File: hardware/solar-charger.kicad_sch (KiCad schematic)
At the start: 24 parts, among them J1 Conn_01x02_Male, J2 ISENSE_SOLAR, J3 ISENSE_SOLAR, J4 ISENSE_SOLAR, J5 ISENSE_DISCHARGE, J6 Conn_01x02_Male, Q1 AOI21357, Q2 AOI21357, Q3 AOI21357, Q4 AOI21357, U1 MCP6002-xP, U2 DS3231M

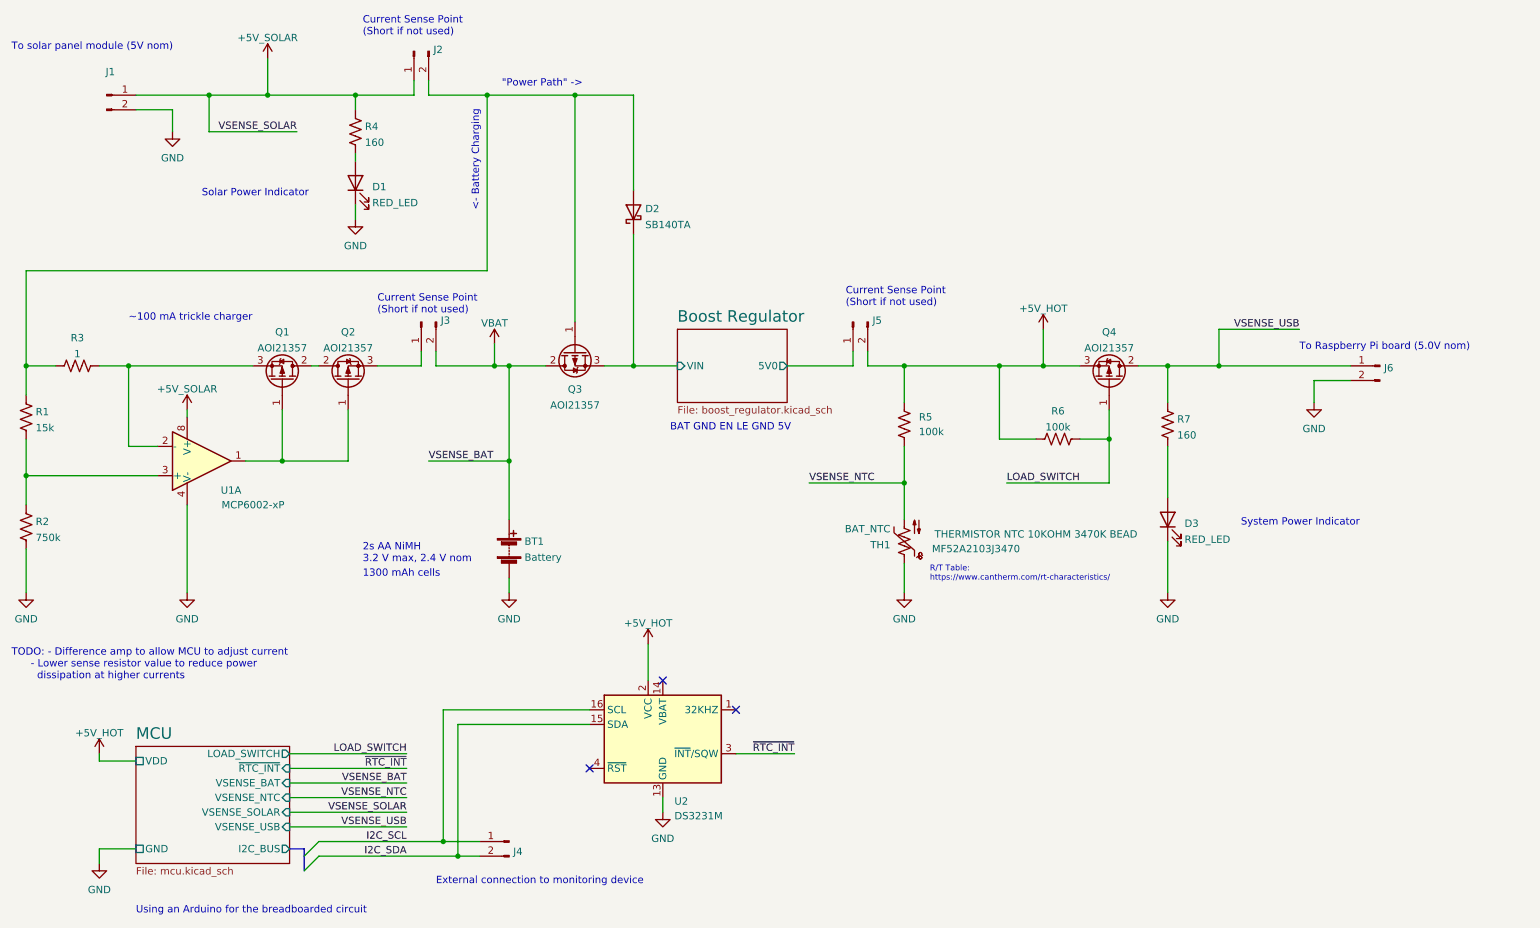
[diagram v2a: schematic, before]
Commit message: hardware: Replace current sense with a schottky, scrap blocking FET Q2
We discovered that we require a diode anyways, so to be a bit more
efficient, replace the fairly large current sense resistor with a
schottky. This required that we updated the voltage divider values to
reflect the new required voltage drop.

Future work here is to consider the worst case highest temperature we
want to support, and then add in a digipot to allow the micro to adjust
the voltage (and therefore the current) up from that point.
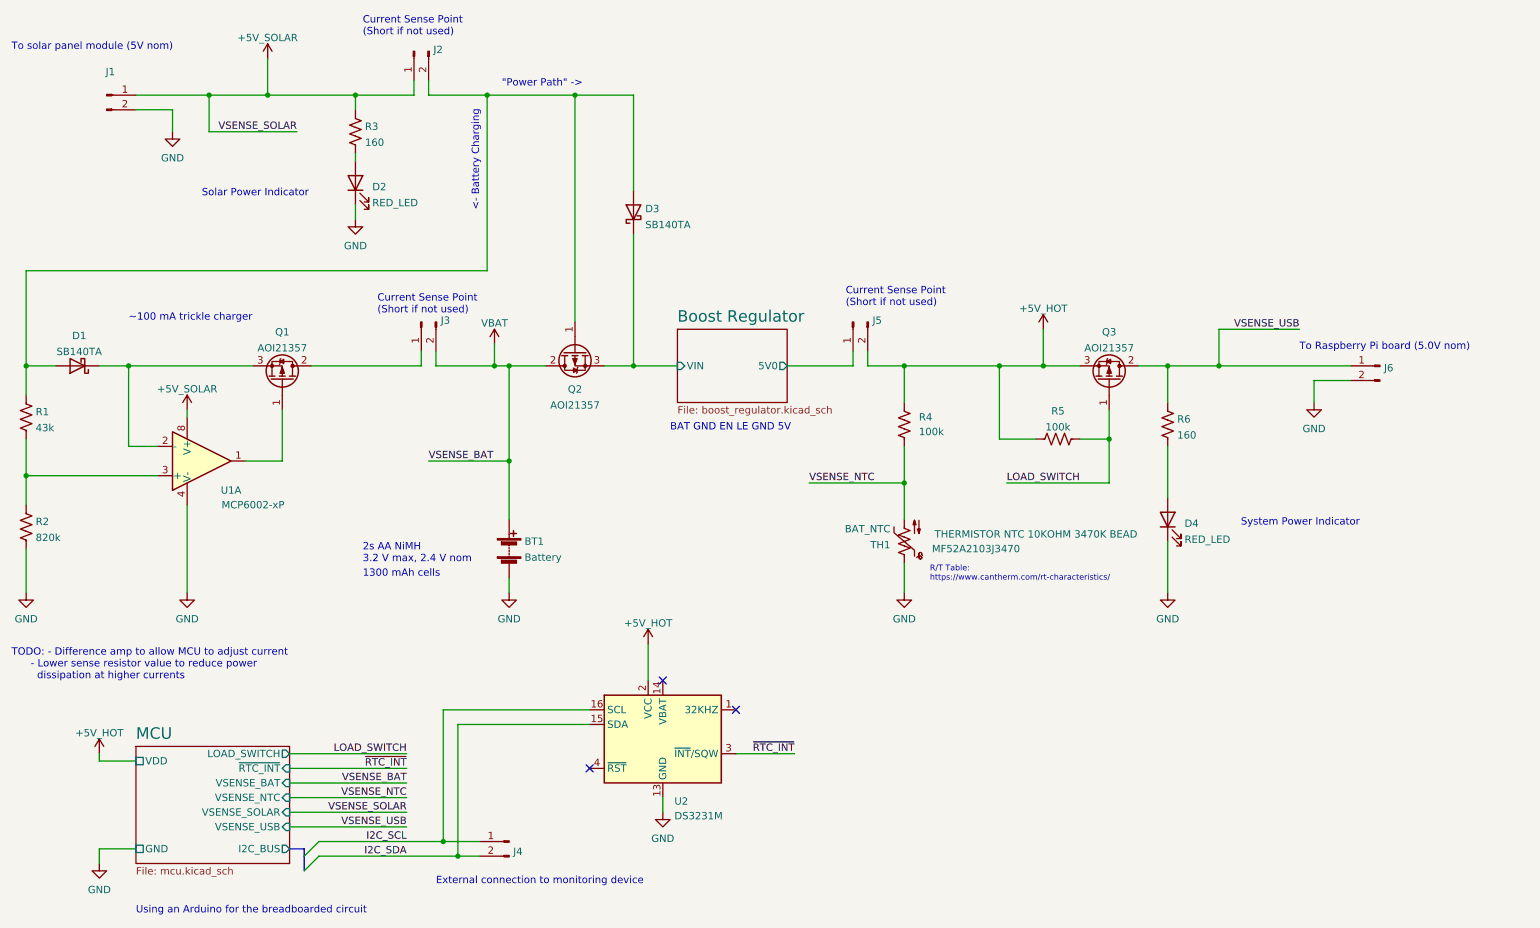
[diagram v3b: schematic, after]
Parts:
- removed Q2: AOI21357, symbol Device:Q_PMOS_GDS
- removed R3: 1, symbol Device:R_US
- added D1: SB140TA, symbol Device:D_Schottky
- R1: value 15k -> 43k
- R2: value 750k -> 820k
- renumbered D1 to D2, D2 to D3, D3 to D4, Q3 to Q2, Q4 to Q3, R4 to R3, R5 to R4, R6 to R5, R7 to R6
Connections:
- net at D3.2 (A), J2.2 (Pin_2), Q2.1 (G)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: now also D1.2 (A)
- net at Q1.3 (S), U1.2 (-): now also D1.1 (K)
- net at Q1.2 (D): now also J3.1 (Pin_1)
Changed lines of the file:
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@@
   (junction (at 232.41 92.71) (diameter 0) (color 0 0 0 0)
-  )
-  (junction (at 69.85 109.22) (diameter 0) (color 0 0 0 0)
   )
   (junction (at 177.8 113.03) (diameter 0) (color 0 0 0 0)
@@
     (stroke (width 0) (type default) (color 0 0 0 0))
   )
-  (wire (pts (xy 81.28 109.22) (xy 81.28 100.33))
-    (stroke (width 0) (type default) (color 0 0 0 0))
-  )
   (wire (pts (xy 125.73 92.71) (xy 130.81 92.71))
     (stroke (width 0) (type default) (color 0 0 0 0))
@@
     (stroke (width 0) (type default) (color 0 0 0 0))
   )
-  (wire (pts (xy 53.34 101.6) (xy 53.34 100.33))
-    (stroke (width 0) (type default) (color 0 0 0 0))
-  )
   (wire (pts (xy 97.79 175.26) (xy 104.14 175.26))
     (stroke (width 0) (type default) (color 0 0 0 0))
@@
     (stroke (width 0) (type default) (color 0 0 0 0))
   )
-  (wire (pts (xy 86.36 92.71) (xy 93.98 92.71))
-    (stroke (width 0) (type default) (color 0 0 0 0))
-  )
   (wire (pts (xy 106.68 92.71) (xy 109.22 92.71))
     (stroke (width 0) (type default) (color 0 0 0 0))
@@
     (stroke (width 0) (type default) (color 0 0 0 0))
   )
+  (wire (pts (xy 53.34 100.33) (xy 53.34 101.6))
+    (stroke (width 0) (type default) (color 0 0 0 0))
+  )
   (wire (pts (xy 57.15 45.72) (xy 57.15 52.07))
     (stroke (width 0) (type default) (color 0 0 0 0))
@@
     (stroke (width 0) (type default) (color 0 0 0 0))
   )
-  (wire (pts (xy 74.93 92.71) (xy 76.2 92.71))
+  (wire (pts (xy 74.93 92.71) (xy 93.98 92.71))
     (stroke (width 0) (type default) (color 0 0 0 0))
   )
@@
   )
   (wire (pts (xy 95.25 43.18) (xy 95.25 45.72))
-    (stroke (width 0) (type default) (color 0 0 0 0))
-  )
-  (wire (pts (xy 69.85 109.22) (xy 81.28 109.22))
     (stroke (width 0) (type default) (color 0 0 0 0))
   )
@@
   )
   (symbol (lib_id "power:+5V_SOLAR") (at 53.34 100.33 0) (unit 1)
-    (in_bom yes) (on_board yes) (fields_autoplaced)
+    (in_bom yes) (on_board yes)
     (property "Reference" "#PWR05" (id 0) (at 53.34 104.14 0)
       (effects (font (size 1.27 1.27)) hide)
@@
   (symbol (lib_id "Device:D_Schottky") (at 130.81 66.04 90) (unit 1)
     (in_bom yes) (on_board yes) (fields_autoplaced)
-    (property "Reference" "D2" (id 0) (at 132.842 65.449 90)
+    (property "Reference" "D3" (id 0) (at 132.842 65.449 90)
       (effects (font (size 1.27 1.27)) (justify right))
     )
@@
       (effects (font (size 1.27 1.27)) (justify left))
     )
-    (property "Value" "15k" (id 1) (at 27.051 103.4666 0)
+    (property "Value" "43k" (id 1) (at 27.051 103.4666 0)
       (effects (font (size 1.27 1.27)) (justify left))
     )
@@
   (symbol (lib_id "Device:R_US") (at 82.55 52.07 0) (unit 1)
     (in_bom yes) (on_board yes) (fields_autoplaced)
-    (property "Reference" "R4" (id 0) (at 84.201 51.1615 0)
+    (property "Reference" "R3" (id 0) (at 84.201 51.1615 0)
       (effects (font (size 1.27 1.27)) (justify left))
     )
@@
   (symbol (lib_id "Device:R_US") (at 177.8 102.87 0) (unit 1)
     (in_bom yes) (on_board yes) (fields_autoplaced)
-    (property "Reference" "R5" (id 0) (at 180.34 101.5999 0)
+    (property "Reference" "R4" (id 0) (at 180.34 101.5999 0)
       (effects (font (size 1.27 1.27)) (justify left))
     )
@@
     (pin "2")
   )
+  (symbol (lib_id "Device:D_Schottky") (at 34.29 92.71 180) (unit 1)
+    (in_bom yes) (on_board yes) (fields_autoplaced)
+    (property "Reference" "D1" (id 0) (at 34.6075 87.4735 0))
+    (property "Value" "SB140TA" (id 1) (at 34.6075 90.2486 0))
+    (property "Footprint" "" (id 2) (at 34.29 92.71 0)
+      (effects (font (size 1.27 1.27)) hide)
+    )
+    (property "Datasheet" "http://www.smc-diodes.com/propdf/SB120%20THRU%20SB160%20N0869%20REV.C.pdf" (id 3) (at 34.29 92.71 0)
+      (effects (font (size 1.27 1.27)) hide)
+    )
+    (pin "1")
+    (pin "2")
+  )
   (symbol (lib_id "Device:Q_PMOS_GDS") (at 213.36 95.25 270) (mirror x) (unit 1)
     (in_bom yes) (on_board yes) (fields_autoplaced)
-    (property "Reference" "Q4" (id 0) (at 213.36 86.8385 90))
+    (property "Reference" "Q3" (id 0) (at 213.36 86.8385 90))
     (property "Value" "AOI21357" (id 1) (at 213.36 89.6136 90))
     (property "Footprint" "" (id 2) (at 215.9 90.17 0)
@@
   (symbol (lib_id "Device:LED") (at 223.52 119.38 90) (unit 1)
     (in_bom yes) (on_board yes) (fields_autoplaced)
-    (property "Reference" "D3" (id 0) (at 226.441 120.059 90)
+    (property "Reference" "D4" (id 0) (at 226.441 120.059 90)
       (effects (font (size 1.27 1.27)) (justify right))
     )
@@
     )
     (property "Datasheet" "~" (id 3) (at 223.52 119.38 0)
-      (effects (font (size 1.27 1.27)) hide)
-    )
-    (pin "1")
-    (pin "2")
-  )
-  (symbol (lib_id "Device:R_US") (at 34.29 92.71 90) (unit 1)
-    (in_bom yes) (on_board yes) (fields_autoplaced)
-    (property "Reference" "R3" (id 0) (at 34.29 87.8545 90))
-    (property "Value" "1" (id 1) (at 34.29 90.6296 90))
-    (property "Footprint" "" (id 2) (at 34.544 91.694 90)
-      (effects (font (size 1.27 1.27)) hide)
-    )
-    (property "Datasheet" "~" (id 3) (at 34.29 92.71 0)
       (effects (font (size 1.27 1.27)) hide)
     )
@@
   (symbol (lib_id "Device:R_US") (at 204.47 105.41 90) (unit 1)
     (in_bom yes) (on_board yes) (fields_autoplaced)
-    (property "Reference" "R6" (id 0) (at 204.47 100.5545 90))
+    (property "Reference" "R5" (id 0) (at 204.47 100.5545 90))
     (property "Value" "100k" (id 1) (at 204.47 103.3296 90))
     (property "Footprint" "" (id 2) (at 204.724 104.394 90)
@@
     )
     (pin "1")
-  )
-  (symbol (lib_id "Device:Q_PMOS_GDS") (at 81.28 95.25 90) (unit 1)
-    (in_bom yes) (on_board yes) (fields_autoplaced)
-    (property "Reference" "Q2" (id 0) (at 81.28 86.8385 90))
-    (property "Value" "AOI21357" (id 1) (at 81.28 89.6136 90))
-    (property "Footprint" "" (id 2) (at 78.74 90.17 0)
-      (effects (font (size 1.27 1.27)) hide)
-    )
-    (property "Datasheet" "~" (id 3) (at 81.28 95.25 0)
-      (effects (font (size 1.27 1.27)) hide)
-    )
-    (pin "1")
-    (pin "2")
-    (pin "3")
   )
   (symbol (lib_id "power:GND") (at 109.22 132.08 0) (unit 1)
@@
   (symbol (lib_id "Device:R_US") (at 223.52 102.87 0) (unit 1)
     (in_bom yes) (on_board yes) (fields_autoplaced)
-    (property "Reference" "R7" (id 0) (at 225.171 101.9615 0)
+    (property "Reference" "R6" (id 0) (at 225.171 101.9615 0)
       (effects (font (size 1.27 1.27)) (justify left))
     )
@@
   (symbol (lib_id "Device:LED") (at 82.55 60.96 90) (unit 1)
     (in_bom yes) (on_board yes) (fields_autoplaced)
-    (property "Reference" "D1" (id 0) (at 85.471 61.639 90)
+    (property "Reference" "D2" (id 0) (at 85.471 61.639 90)
       (effects (font (size 1.27 1.27)) (justify right))
     )
@@
   (symbol (lib_id "Device:Q_PMOS_GDS") (at 120.65 90.17 90) (mirror x) (unit 1)
     (in_bom yes) (on_board yes) (fields_autoplaced)
-    (property "Reference" "Q3" (id 0) (at 120.65 96.7645 90))
+    (property "Reference" "Q2" (id 0) (at 120.65 96.7645 90))
     (property "Value" "AOI21357" (id 1) (at 120.65 99.5396 90))
     (property "Footprint" "" (id 2) (at 118.11 95.25 0)
@@
       (effects (font (size 1.27 1.27)) (justify left))
     )
-    (property "Value" "750k" (id 1) (at 27.051 122.5166 0)
+    (property "Value" "820k" (id 1) (at 27.051 122.5166 0)
       (effects (font (size 1.27 1.27)) (justify left))
     )
@@
       (reference "BT1") (unit 1) (value "Battery") (footprint "")
     )
+    (path "/30373759-5cc3-429e-89ca-e3d615395bd9"
+      (reference "D1") (unit 1) (value "SB140TA") (footprint "")
+    )
     (path "/967f21db-49b4-43ea-8bae-37ea91ee0186"
-      (reference "D1") (unit 1) (value "RED_LED") (footprint "")
+      (reference "D2") (unit 1) (value "RED_LED") (footprint "")
     )
     (path "/1e2c537e-fa7d-49c7-a8c9-3a176b9f0858"
-      (reference "D2") (unit 1) (value "SB140TA") (footprint "")
+      (reference "D3") (unit 1) (value "SB140TA") (footprint "")
     )
     (path "/4fd70c75-2c71-4b29-843c-8d9ca9355a76"
-      (reference "D3") (unit 1) (value "RED_LED") (footprint "")
+      (reference "D4") (unit 1) (value "RED_LED") (footprint "")
     )
     (path "/4b77a933-4d0b-41f7-957c-3b62091c625b"
@@
       (reference "Q1") (unit 1) (value "AOI21357") (footprint "")
     )
-    (path "/7d62a127-2980-416f-9433-e6276e6cc82e"
+    (path "/cd9af8bc-e480-49c0-936f-b0e08cea1433"
       (reference "Q2") (unit 1) (value "AOI21357") (footprint "")
     )
-    (path "/cd9af8bc-e480-49c0-936f-b0e08cea1433"
+    (path "/44fffe8f-5192-4680-ab1c-b77de28a9431"
       (reference "Q3") (unit 1) (value "AOI21357") (footprint "")
     )
-    (path "/44fffe8f-5192-4680-ab1c-b77de28a9431"
-      (reference "Q4") (unit 1) (value "AOI21357") (footprint "")
-    )
     (path "/27c6cc50-ac41-453f-8f74-90611a703dbb"
-      (reference "R1") (unit 1) (value "15k") (footprint "")
+      (reference "R1") (unit 1) (value "43k") (footprint "")
     )
     (path "/f1c4192e-738f-41d6-a0ec-8dd6c1776085"
-      (reference "R2") (unit 1) (value "750k") (footprint "")
-    )
-    (path "/56f90a98-4f73-4018-a49b-93c7f3f3aadc"
-      (reference "R3") (unit 1) (value "1") (footprint "")
+      (reference "R2") (unit 1) (value "820k") (footprint "")
     )
     (path "/28ab08ba-bf6c-461d-bfe3-5e410b6f9659"
-      (reference "R4") (unit 1) (value "160") (footprint "")
+      (reference "R3") (unit 1) (value "160") (footprint "")
     )
     (path "/2f085b0f-8ffd-4730-997c-84fa669cb96f"
+      (reference "R4") (unit 1) (value "100k") (footprint "")
+    )
+    (path "/6bdb21b9-d941-45b1-85c2-94aa3b64b1e6"
       (reference "R5") (unit 1) (value "100k") (footprint "")
     )
-    (path "/6bdb21b9-d941-45b1-85c2-94aa3b64b1e6"
-      (reference "R6") (unit 1) (value "100k") (footprint "")
-    )
     (path "/8df32837-f0cb-40b4-839c-21264f0a9b65"
-      (reference "R7") (unit 1) (value "160") (footprint "")
+      (reference "R6") (unit 1) (value "160") (footprint "")
     )
     (path "/d4a5292d-9b11-4f65-9728-981f1120df99"
